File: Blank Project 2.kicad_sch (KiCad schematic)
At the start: 13 parts

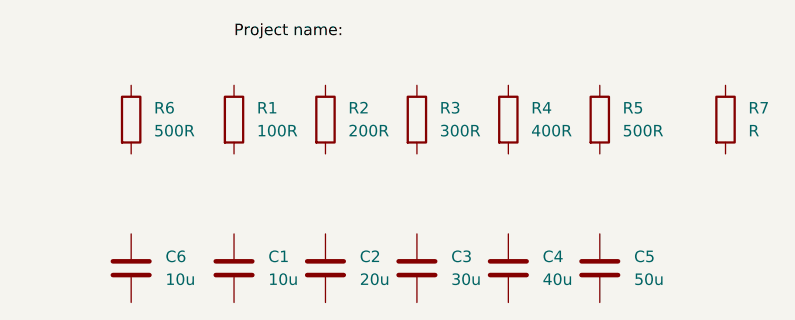
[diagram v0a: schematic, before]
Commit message: Added R8
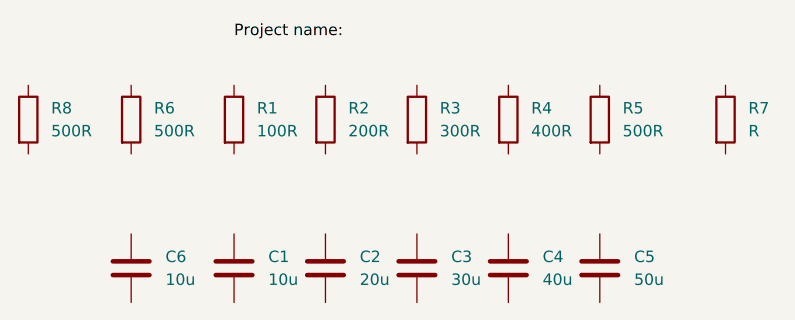
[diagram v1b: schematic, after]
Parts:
- added R8: 500R, symbol Device:R
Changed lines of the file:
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@@
     (effects (font (size 1.27 1.27)) (justify left bottom))
+  )
+  (symbol (lib_id "Device:R") (at 106.68 119.38 0) (unit 1)
+    (in_bom yes) (on_board yes) (fields_autoplaced)
+    (property "Reference" "R8" (id 0) (at 109.22 118.1099 0)
+      (effects (font (size 1.27 1.27)) (justify left))
+    )
+    (property "Value" "500R" (id 1) (at 109.22 120.6499 0)
+      (effects (font (size 1.27 1.27)) (justify left))
+    )
+    (property "Footprint" "" (id 2) (at 104.902 119.38 90)
+      (effects (font (size 1.27 1.27)) hide)
+    )
+    (property "Datasheet" "~" (id 3) (at 106.68 119.38 0)
+      (effects (font (size 1.27 1.27)) hide)
+    )
+    (pin "1")
+    (pin "2")
   )
   (symbol (lib_id "Device:R") (at 118.11 119.38 0) (unit 1)
@@
       (reference "R7") (unit 1) (value "R") (footprint "")
     )
-  )
+    (path "/8de3db44-673f-4dd7-8a1e-fe57b7d92a77"
+      (reference "R8") (unit 1) (value "500R") (footprint "")
+    )
+  )

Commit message: Deleted R8.
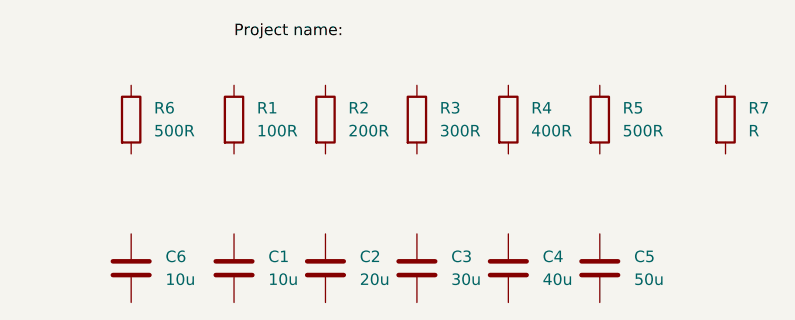
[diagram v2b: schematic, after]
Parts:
- removed R8: 500R, symbol Device:R
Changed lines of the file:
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@@
     (effects (font (size 1.27 1.27)) (justify left bottom))
-  )
-  (symbol (lib_id "Device:R") (at 106.68 119.38 0) (unit 1)
-    (in_bom yes) (on_board yes) (fields_autoplaced)
-    (property "Reference" "R8" (id 0) (at 109.22 118.1099 0)
-      (effects (font (size 1.27 1.27)) (justify left))
-    )
-    (property "Value" "500R" (id 1) (at 109.22 120.6499 0)
-      (effects (font (size 1.27 1.27)) (justify left))
-    )
-    (property "Footprint" "" (id 2) (at 104.902 119.38 90)
-      (effects (font (size 1.27 1.27)) hide)
-    )
-    (property "Datasheet" "~" (id 3) (at 106.68 119.38 0)
-      (effects (font (size 1.27 1.27)) hide)
-    )
-    (pin "1")
-    (pin "2")
   )
   (symbol (lib_id "Device:R") (at 118.11 119.38 0) (unit 1)
@@
       (reference "R7") (unit 1) (value "R") (footprint "")
     )
-    (path "/8de3db44-673f-4dd7-8a1e-fe57b7d92a77"
-      (reference "R8") (unit 1) (value "500R") (footprint "")
-    )
-  )
+  )
